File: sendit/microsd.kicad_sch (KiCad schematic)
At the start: 10 parts, among them J9 Micro_SD_Card

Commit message: bigger update
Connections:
- no-connect marks 0 -> 2
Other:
- moved on the sheet: J9, R60, R61, R62, R63, R64, R65, R66, R67

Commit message: layout work.
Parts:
- renumbered C21 to C16, J9 to J25, R60 to R69, R61 to R70, R62 to R71, R63 to R72, R67 to R73, R65 to R74, R64 to R75, R66 to R76
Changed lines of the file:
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@@
 		(on_board yes)
 		(dnp no)
-		(property "Reference" "R65"
+		(property "Reference" "R74"
 			(at 167.64 99.314 90)
 			(effects
@@
 			(project "sendit"
 				(path "/a355e4d0-2918-44fc-be8d-2503b84c6d6c/a39a4809-b17d-4cec-8315-6a7318917ec7"
-					(reference "R65")
+					(reference "R74")
 					(unit 1)
 				)
@@
 		(dnp no)
 		(fields_autoplaced yes)
-		(property "Reference" "#PWR0104"
+		(property "Reference" "#PWR0102"
 			(at 100.33 83.82 0)
 			(effects
@@
 			(project "sendit"
 				(path "/a355e4d0-2918-44fc-be8d-2503b84c6d6c/a39a4809-b17d-4cec-8315-6a7318917ec7"
-					(reference "#PWR0104")
+					(reference "#PWR0102")
 					(unit 1)
 				)
@@
 		(dnp no)
 		(fields_autoplaced yes)
-		(property "Reference" "J9"
+		(property "Reference" "J25"
 			(at 202.565 83.82 0)
 			(effects
@@
 			(project ""
 				(path "/a355e4d0-2918-44fc-be8d-2503b84c6d6c/a39a4809-b17d-4cec-8315-6a7318917ec7"
-					(reference "J9")
+					(reference "J25")
 					(unit 1)
 				)
@@
 		(on_board yes)
 		(dnp no)
-		(property "Reference" "R64"
+		(property "Reference" "R75"
 			(at 167.64 104.394 90)
 			(effects
@@
 			(project "sendit"
 				(path "/a355e4d0-2918-44fc-be8d-2503b84c6d6c/a39a4809-b17d-4cec-8315-6a7318917ec7"
-					(reference "R64")
+					(reference "R75")
 					(unit 1)
 				)
@@
 		(dnp no)
 		(fields_autoplaced yes)
-		(property "Reference" "R60"
+		(property "Reference" "R69"
 			(at 125.73 87.6299 0)
 			(effects
@@
 			(project "sendit"
 				(path "/a355e4d0-2918-44fc-be8d-2503b84c6d6c/a39a4809-b17d-4cec-8315-6a7318917ec7"
-					(reference "R60")
+					(reference "R69")
 					(unit 1)
 				)
@@
 		(dnp no)
 		(fields_autoplaced yes)
-		(property "Reference" "R61"
+		(property "Reference" "R70"
 			(at 134.62 87.6299 0)
 			(effects
@@
 			(project "sendit"
 				(path "/a355e4d0-2918-44fc-be8d-2503b84c6d6c/a39a4809-b17d-4cec-8315-6a7318917ec7"
-					(reference "R61")
+					(reference "R70")
 					(unit 1)
 				)
@@
 		(dnp no)
 		(fields_autoplaced yes)
-		(property "Reference" "#PWR0105"
+		(property "Reference" "#PWR0103"
 			(at 100.33 134.62 0)
 			(effects
@@
 			(project "sendit"
 				(path "/a355e4d0-2918-44fc-be8d-2503b84c6d6c/a39a4809-b17d-4cec-8315-6a7318917ec7"
-					(reference "#PWR0105")
+					(reference "#PWR0103")
 					(unit 1)
 				)
@@
 		(dnp no)
 		(fields_autoplaced yes)
-		(property "Reference" "R62"
+		(property "Reference" "R71"
 			(at 143.51 87.6299 0)
 			(effects
@@
 			(project "sendit"
 				(path "/a355e4d0-2918-44fc-be8d-2503b84c6d6c/a39a4809-b17d-4cec-8315-6a7318917ec7"
-					(reference "R62")
+					(reference "R71")
 					(unit 1)
 				)
@@
 		(on_board yes)
 		(dnp no)
-		(property "Reference" "C21"
+		(property "Reference" "C16"
 			(at 102.87 104.1463 0)
 			(effects
@@
 			(project "sendit"
 				(path "/a355e4d0-2918-44fc-be8d-2503b84c6d6c/a39a4809-b17d-4cec-8315-6a7318917ec7"
-					(reference "C21")
+					(reference "C16")
 					(unit 1)
 				)
@@
 		(on_board yes)
 		(dnp no)
-		(property "Reference" "R66"
+		(property "Reference" "R76"
 			(at 167.64 109.474 90)
 			(effects
@@
 			(project "sendit"
 				(path "/a355e4d0-2918-44fc-be8d-2503b84c6d6c/a39a4809-b17d-4cec-8315-6a7318917ec7"
-					(reference "R66")
+					(reference "R76")
 					(unit 1)
 				)
@@
 		(dnp no)
 		(fields_autoplaced yes)
-		(property "Reference" "R63"
+		(property "Reference" "R72"
 			(at 152.4 87.6299 0)
 			(effects
@@
 			(project "sendit"
 				(path "/a355e4d0-2918-44fc-be8d-2503b84c6d6c/a39a4809-b17d-4cec-8315-6a7318917ec7"
-					(reference "R63")
+					(reference "R72")
 					(unit 1)
 				)
@@
 		(dnp no)
 		(fields_autoplaced yes)
-		(property "Reference" "R67"
+		(property "Reference" "R73"
 			(at 161.29 87.6299 0)
 			(effects
@@
 			(project "sendit"
 				(path "/a355e4d0-2918-44fc-be8d-2503b84c6d6c/a39a4809-b17d-4cec-8315-6a7318917ec7"
-					(reference "R67")
-					(unit 1)
-				)
+					(reference "R73")
+					(unit 1)
+				)

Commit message: updated footprints and lcsc numbers.
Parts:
- C16: footprint Capacitor_SMD:C_0805_2012Metric_Pad1.18x1.45mm_HandSolder -> Capacitor_SMD:C_0603_1608Metric; LCSC (none) -> C19702
- J25: symbol Connector:Micro_SD_Card_Det1 -> Connector:Micro_SD_Card_Det_Hirose_DM3AT; LCSC (none) -> C114218
- R69, R70, R71, R72, R74, R75, R76: footprint Resistor_SMD:R_0805_2012Metric_Pad1.20x1.40mm_HandSolder -> Resistor_SMD:R_0603_1608Metric
- R73: value 10k -> 4.7k; footprint Resistor_SMD:R_0805_2012Metric_Pad1.20x1.40mm_HandSolder -> Resistor_SMD:R_0603_1608Metric
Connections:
- net DETECT: no longer R73.1
- net GND: now also J25.11 (SHIELD); no longer J25.10 (SHIELD)
- new net: J25.10 (DET_A), R73.1
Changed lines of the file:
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@@
-	)
-	(junction
-		(at 158.75 118.11)
-		(diameter 0)
-		(color 0 0 0 0)
 	)
 	(junction
@@
 	(wire
 		(pts
-			(xy 158.75 118.11) (xy 158.75 91.44)
-		)
-		(stroke
-			(width 0)
-			(type default)
-		)
-	)
-	(wire
-		(pts
 			(xy 132.08 81.28) (xy 123.19 81.28)
 		)
@@
 	(wire
 		(pts
-			(xy 179.07 118.11) (xy 158.75 118.11)
+			(xy 116.84 118.11) (xy 179.07 118.11)
 		)
 		(stroke
@@
 	(wire
 		(pts
-			(xy 116.84 118.11) (xy 158.75 118.11)
-		)
-		(stroke
-			(width 0)
-			(type default)
-		)
-	)
-	(wire
-		(pts
 			(xy 123.19 97.79) (xy 179.07 97.79)
 		)
@@
 	(wire
 		(pts
+			(xy 158.75 115.57) (xy 179.07 115.57)
+		)
+		(stroke
+			(width 0)
+			(type default)
+		)
+	)
+	(wire
+		(pts
 			(xy 100.33 81.28) (xy 100.33 80.01)
 		)
@@
 		(pts
 			(xy 123.19 81.28) (xy 123.19 86.36)
+		)
+		(stroke
+			(width 0)
+			(type default)
+		)
+	)
+	(wire
+		(pts
+			(xy 158.75 115.57) (xy 158.75 91.44)
 		)
 		(stroke
@@
 			)
 		)
-		(property "Footprint" "Resistor_SMD:R_0805_2012Metric_Pad1.20x1.40mm_HandSolder"
+		(property "Footprint" "Resistor_SMD:R_0603_1608Metric"
 			(at 171.45 100.33 0)
 			(effects
@@
 	)
 	(symbol
-		(lib_id "Connector:Micro_SD_Card_Det1")
+		(lib_id "Connector:Micro_SD_Card_Det_Hirose_DM3AT")
 		(at 201.93 105.41 0)
 		(unit 1)
@@
 			)
 		)
-		(property "Datasheet" "https://datasheet.lcsc.com/lcsc/2110151630_XKB-Connectivity-XKTF-015-N_C381082.pdf"
+		(property "Datasheet" "https://www.hirose.com/product/en/download_file/key_name/DM3/category/Catalog/doc_file_id/49662/?file_category_id=4&item_id=195&is_series=1"
 			(at 201.93 102.87 0)
 			(effects
@@
 			)
 		)
-		(property "Description" "Micro SD Card Socket with one card detection pin"
+		(property "Description" "Micro SD Card Socket with card detection pins"
 			(at 201.93 105.41 0)
 			(effects
@@
 			)
 		)
+		(property "LCSC" "C114218"
+			(at 201.93 105.41 0)
+			(effects
+				(font
+					(size 1.27 1.27)
+				)
+				(hide yes)
+			)
+		)
 		(pin "1"
 		)
@@
 		)
 		(pin "10"
+		)
+		(pin "11"
 		)
 		(instances
@@
 			)
 		)
-		(property "Footprint" "Resistor_SMD:R_0805_2012Metric_Pad1.20x1.40mm_HandSolder"
+		(property "Footprint" "Resistor_SMD:R_0603_1608Metric"
 			(at 171.45 105.41 0)
 			(effects
@@
 			)
 		)
-		(property "Footprint" "Resistor_SMD:R_0805_2012Metric_Pad1.20x1.40mm_HandSolder"
+		(property "Footprint" "Resistor_SMD:R_0603_1608Metric"
 			(at 123.19 88.9 0)
 			(effects
@@
 			)
 		)
-		(property "Footprint" "Resistor_SMD:R_0805_2012Metric_Pad1.20x1.40mm_HandSolder"
+		(property "Footprint" "Resistor_SMD:R_0603_1608Metric"
 			(at 132.08 88.9 0)
 			(effects
@@
 			)
 		)
-		(property "Footprint" "Resistor_SMD:R_0805_2012Metric_Pad1.20x1.40mm_HandSolder"
+		(property "Footprint" "Resistor_SMD:R_0603_1608Metric"
 			(at 140.97 88.9 0)
 			(effects
@@
 			)
 		)
-		(property "Footprint" "Capacitor_SMD:C_0805_2012Metric_Pad1.18x1.45mm_HandSolder"
+		(property "Footprint" "Capacitor_SMD:C_0603_1608Metric"
 			(at 100.33 105.41 0)
 			(effects
@@
 			)
 		)
-		(property "LCSC" ""
+		(property "LCSC" "C19702"
 			(at 100.33 105.41 0)
 			(effects
@@
 			)
 		)
-		(property "Footprint" "Resistor_SMD:R_0805_2012Metric_Pad1.20x1.40mm_HandSolder"
+		(property "Footprint" "Resistor_SMD:R_0603_1608Metric"
 			(at 171.45 110.49 0)
 			(effects
@@
 			)
 		)
-		(property "Footprint" "Resistor_SMD:R_0805_2012Metric_Pad1.20x1.40mm_HandSolder"
+		(property "Footprint" "Resistor_SMD:R_0603_1608Metric"
 			(at 149.86 88.9 0)
 			(effects
@@
 			)
 		)
-		(property "Value" "10k"
+		(property "Value" "4.7k"
 			(at 161.29 90.1699 0)
 			(effects
@@
 			)
 		)
-		(property "Footprint" "Resistor_SMD:R_0805_2012Metric_Pad1.20x1.40mm_HandSolder"
+		(property "Footprint" "Resistor_SMD:R_0603_1608Metric"
 			(at 158.75 88.9 0)
 			(effects

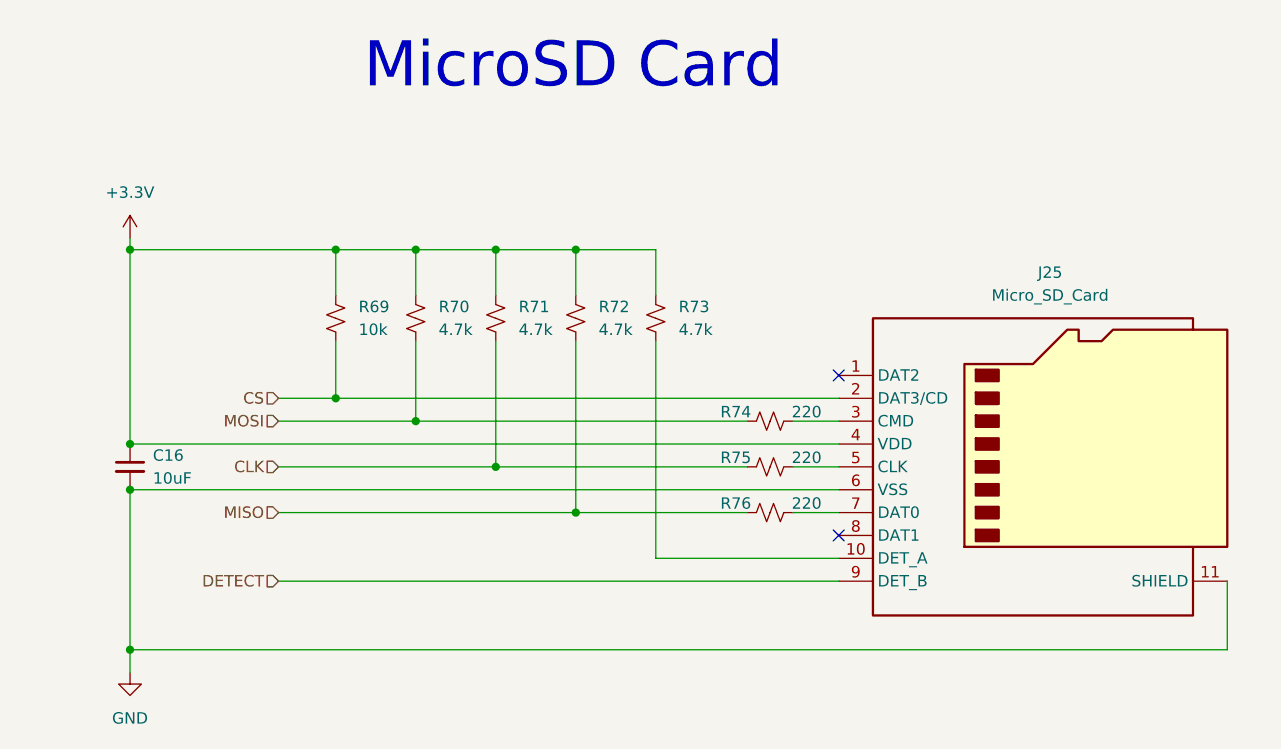
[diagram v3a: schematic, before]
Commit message: test run of jlcpcb upload looks good.
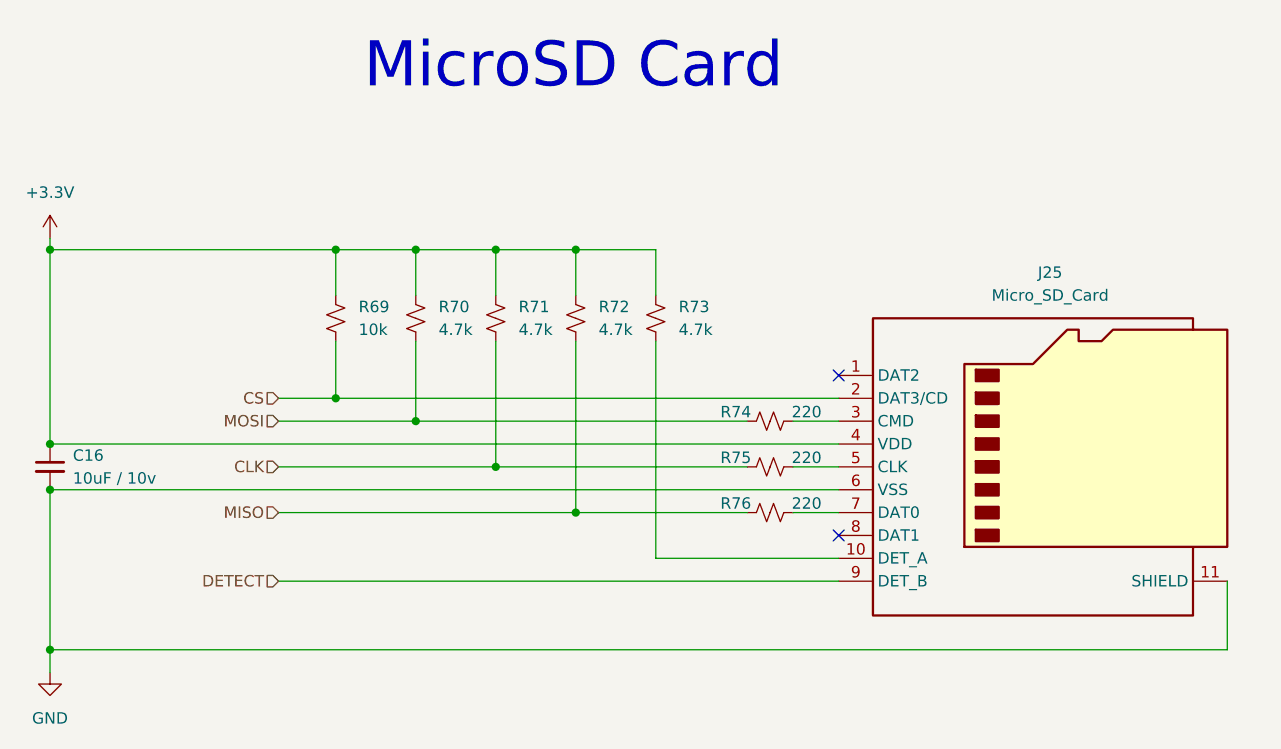
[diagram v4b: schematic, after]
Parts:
- C16: value 10uF -> 10uF / 10v
- R69: LCSC (none) -> C25804
- R70, R71, R72, R73: LCSC (none) -> C23162
- R74, R75, R76: LCSC (none) -> C22962
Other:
- moved on the sheet: C16
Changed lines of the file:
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@@
 	)
 	(junction
-		(at 100.33 102.87)
+		(at 91.44 102.87)
 		(diameter 0)
 		(color 0 0 0 0)
 	)
 	(junction
-		(at 100.33 125.73)
+		(at 91.44 125.73)
 		(diameter 0)
 		(color 0 0 0 0)
@@
 	)
 	(junction
-		(at 100.33 81.28)
+		(at 91.44 81.28)
 		(diameter 0)
 		(color 0 0 0 0)
@@
 	)
 	(junction
-		(at 100.33 107.95)
+		(at 91.44 107.95)
 		(diameter 0)
 		(color 0 0 0 0)
@@
 	(wire
 		(pts
-			(xy 179.07 107.95) (xy 100.33 107.95)
+			(xy 179.07 107.95) (xy 91.44 107.95)
 		)
 		(stroke
@@
 	(wire
 		(pts
-			(xy 100.33 125.73) (xy 100.33 128.27)
+			(xy 91.44 125.73) (xy 91.44 128.27)
 		)
 		(stroke
@@
 	(wire
 		(pts
-			(xy 100.33 81.28) (xy 123.19 81.28)
+			(xy 91.44 81.28) (xy 123.19 81.28)
 		)
 		(stroke
@@
 	(wire
 		(pts
-			(xy 100.33 125.73) (xy 222.25 125.73)
+			(xy 91.44 125.73) (xy 222.25 125.73)
 		)
 		(stroke
@@
 	(wire
 		(pts
-			(xy 100.33 81.28) (xy 100.33 80.01)
+			(xy 91.44 81.28) (xy 91.44 80.01)
 		)
 		(stroke
@@
 	(wire
 		(pts
-			(xy 100.33 107.95) (xy 100.33 125.73)
+			(xy 91.44 107.95) (xy 91.44 125.73)
 		)
 		(stroke
@@
 	(wire
 		(pts
-			(xy 179.07 102.87) (xy 100.33 102.87)
-		)
-		(stroke
-			(width 0)
-			(type default)
-		)
-	)
-	(wire
-		(pts
-			(xy 100.33 102.87) (xy 100.33 81.28)
+			(xy 179.07 102.87) (xy 91.44 102.87)
+		)
+		(stroke
+			(width 0)
+			(type default)
+		)
+	)
+	(wire
+		(pts
+			(xy 91.44 102.87) (xy 91.44 81.28)
 		)
 		(stroke
@@
 			)
 		)
-		(property "LCSC" ""
+		(property "LCSC" "C22962"
 			(at 171.45 100.33 0)
 			(effects
@@
 	(symbol
 		(lib_id "power:+3.3V")
-		(at 100.33 80.01 0)
+		(at 91.44 80.01 0)
 		(unit 1)
 		(exclude_from_sim no)
@@
 		(fields_autoplaced yes)
 		(property "Reference" "#PWR0102"
-			(at 100.33 83.82 0)
+			(at 91.44 83.82 0)
 			(effects
 				(font
@@
 		)
 		(property "Value" "+3.3V"
-			(at 100.33 74.93 0)
+			(at 91.44 74.93 0)
 			(effects
 				(font
@@
 		)
 		(property "Footprint" ""
-			(at 100.33 80.01 0)
+			(at 91.44 80.01 0)
 			(effects
 				(font
@@
 		)
 		(property "Datasheet" ""
-			(at 100.33 80.01 0)
+			(at 91.44 80.01 0)
 			(effects
 				(font
@@
 		)
 		(property "Description" "Power symbol creates a global label with name \"+3.3V\""
-			(at 100.33 80.01 0)
+			(at 91.44 80.01 0)
 			(effects
 				(font
@@
 			)
 		)
-		(property "LCSC" ""
+		(property "LCSC" "C22962"
 			(at 171.45 105.41 0)
 			(effects
@@
 			)
 		)
-		(property "LCSC" ""
+		(property "LCSC" "C25804"
 			(at 123.19 88.9 0)
 			(effects
@@
 			)
 		)
-		(property "LCSC" ""
+		(property "LCSC" "C23162"
 			(at 132.08 88.9 0)
 			(effects
@@
 	(symbol
 		(lib_id "power:GND")
-		(at 100.33 128.27 0)
+		(at 91.44 128.27 0)
 		(unit 1)
 		(exclude_from_sim no)
@@
 		(fields_autoplaced yes)
 		(property "Reference" "#PWR0103"
-			(at 100.33 134.62 0)
+			(at 91.44 134.62 0)
 			(effects
 				(font
@@
 		)
 		(property "Value" "GND"
-			(at 100.33 133.35 0)
+			(at 91.44 133.35 0)
 			(effects
 				(font
@@
 		)
 		(property "Footprint" ""
-			(at 100.33 128.27 0)
+			(at 91.44 128.27 0)
 			(effects
 				(font
@@
 		)
 		(property "Datasheet" ""
-			(at 100.33 128.27 0)
+			(at 91.44 128.27 0)
 			(effects
 				(font
@@
 		)
 		(property "Description" "Power symbol creates a global label with name \"GND\" , ground"
-			(at 100.33 128.27 0)
+			(at 91.44 128.27 0)
 			(effects
 				(font
@@
 			)
 		)
-		(property "LCSC" ""
+		(property "LCSC" "C23162"
 			(at 140.97 88.9 0)
 			(effects
@@
 	(symbol
 		(lib_id "Device:C_Small")
-		(at 100.33 105.41 0)
+		(at 91.44 105.41 0)
 		(unit 1)
 		(exclude_from_sim no)
@@
 		(dnp no)
 		(property "Reference" "C16"
-			(at 102.87 104.1463 0)
+			(at 93.98 104.1463 0)
 			(effects
 				(font
@@
 			)
 		)
-		(property "Value" "10uF"
-			(at 102.87 106.6863 0)
+		(property "Value" "10uF / 10v"
+			(at 93.98 106.6863 0)
 			(effects
 				(font
@@
 		)
 		(property "Footprint" "Capacitor_SMD:C_0603_1608Metric"
-			(at 100.33 105.41 0)
+			(at 91.44 105.41 0)
 			(effects
 				(font
@@
 		)
 		(property "Datasheet" "~"
-			(at 100.33 105.41 0)
+			(at 91.44 105.41 0)
 			(effects
 				(font
@@
 		)
 		(property "Description" ""
-			(at 100.33 105.41 0)
+			(at 91.44 105.41 0)
 			(effects
 				(font
@@
 		)
 		(property "Mouser" ""
-			(at 100.33 105.41 0)
+			(at 91.44 105.41 0)
 			(effects
 				(font
@@
 		)
 		(property "LCSC" "C19702"
-			(at 100.33 105.41 0)
+			(at 91.44 105.41 0)
 			(effects
 				(font
@@
 			)
 		)
-		(property "LCSC" ""
+		(property "LCSC" "C22962"
 			(at 171.45 110.49 0)
 			(effects
@@
 			)
 		)
-		(property "LCSC" ""
+		(property "LCSC" "C23162"
 			(at 149.86 88.9 0)
 			(effects
@@
 			)
 		)
-		(property "LCSC" ""
+		(property "LCSC" "C23162"
 			(at 158.75 88.9 0)
 			(effects

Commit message: fully routed again.
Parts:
- R73: value 4.7k -> 10k
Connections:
- net DETECT: now also J25.10 (DET_A), R73.1; no longer J25.9 (DET_B)
- net GND: now also J25.9 (DET_B)
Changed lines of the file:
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@@
+	)
+	(junction
+		(at 158.75 115.57)
+		(diameter 0)
+		(color 0 0 0 0)
 	)
 	(junction
@@
 		(color 0 0 0 0)
 	)
+	(junction
+		(at 158.75 125.73)
+		(diameter 0)
+		(color 0 0 0 0)
+	)
 	(no_connect
 		(at 179.07 95.25)
@@
 	(wire
 		(pts
-			(xy 116.84 118.11) (xy 179.07 118.11)
+			(xy 116.84 115.57) (xy 158.75 115.57)
 		)
 		(stroke
@@
 	(wire
 		(pts
+			(xy 158.75 91.44) (xy 158.75 115.57)
+		)
+		(stroke
+			(width 0)
+			(type default)
+		)
+	)
+	(wire
+		(pts
 			(xy 149.86 110.49) (xy 168.91 110.49)
 		)
@@
 	(wire
 		(pts
+			(xy 158.75 118.11) (xy 179.07 118.11)
+		)
+		(stroke
+			(width 0)
+			(type default)
+		)
+	)
+	(wire
+		(pts
 			(xy 222.25 118.11) (xy 222.25 125.73)
 		)
@@
 	(wire
 		(pts
-			(xy 91.44 125.73) (xy 222.25 125.73)
+			(xy 91.44 125.73) (xy 158.75 125.73)
+		)
+		(stroke
+			(width 0)
+			(type default)
+		)
+	)
+	(wire
+		(pts
+			(xy 158.75 115.57) (xy 179.07 115.57)
+		)
+		(stroke
+			(width 0)
+			(type default)
+		)
+	)
+	(wire
+		(pts
+			(xy 158.75 118.11) (xy 158.75 125.73)
 		)
 		(stroke
@@
 	(wire
 		(pts
-			(xy 158.75 115.57) (xy 179.07 115.57)
-		)
-		(stroke
-			(width 0)
-			(type default)
-		)
-	)
-	(wire
-		(pts
 			(xy 91.44 81.28) (xy 91.44 80.01)
 		)
@@
 	(wire
 		(pts
-			(xy 158.75 115.57) (xy 158.75 91.44)
-		)
-		(stroke
-			(width 0)
-			(type default)
-		)
-	)
-	(wire
-		(pts
 			(xy 91.44 107.95) (xy 91.44 125.73)
 		)
@@
 		(pts
 			(xy 91.44 102.87) (xy 91.44 81.28)
+		)
+		(stroke
+			(width 0)
+			(type default)
+		)
+	)
+	(wire
+		(pts
+			(xy 158.75 125.73) (xy 222.25 125.73)
 		)
 		(stroke
@@
 	(hierarchical_label "DETECT"
 		(shape input)
-		(at 116.84 118.11 180)
+		(at 116.84 115.57 180)
 		(effects
 			(font
@@
 			)
 		)
-		(property "Value" "4.7k"
+		(property "Value" "10k"
 			(at 161.29 90.1699 0)
 			(effects

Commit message: Rev-A sent to production.
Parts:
- R73: LCSC C23162 -> C25804
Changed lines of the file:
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@@
 			)
 		)
-		(property "LCSC" "C23162"
+		(property "LCSC" "C25804"
 			(at 158.75 88.9 0)
 			(effects
